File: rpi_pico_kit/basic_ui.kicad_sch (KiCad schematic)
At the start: 48 parts, among them Q3 BSS138, Q4 BSS138, Q5 BSS138, Q6 BSS138, SW2 RotaryEncoder_Switch, SW3 SW_Push, SW4 SW_Push, SW5 SW_Push, SW6 SW_Push, U5 74HC14

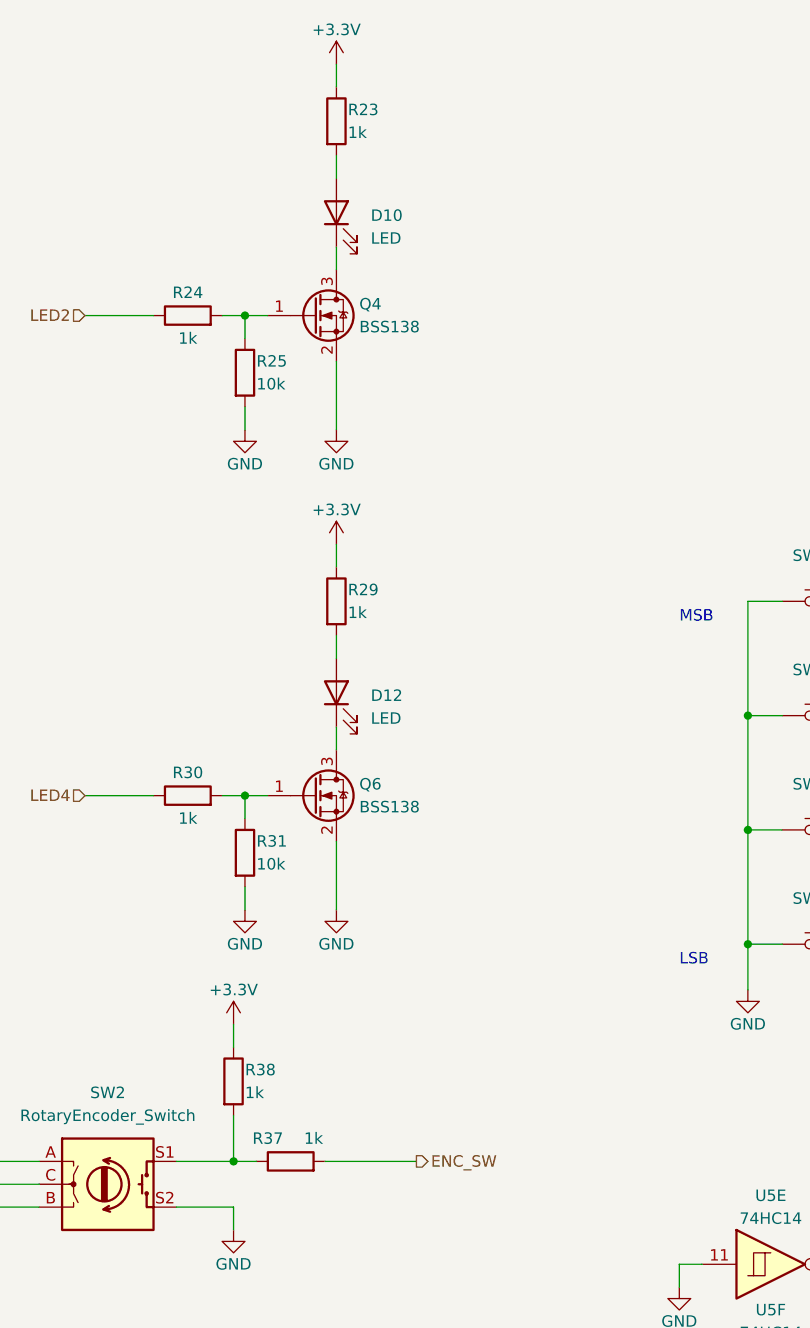
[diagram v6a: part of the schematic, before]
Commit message: changed pinout
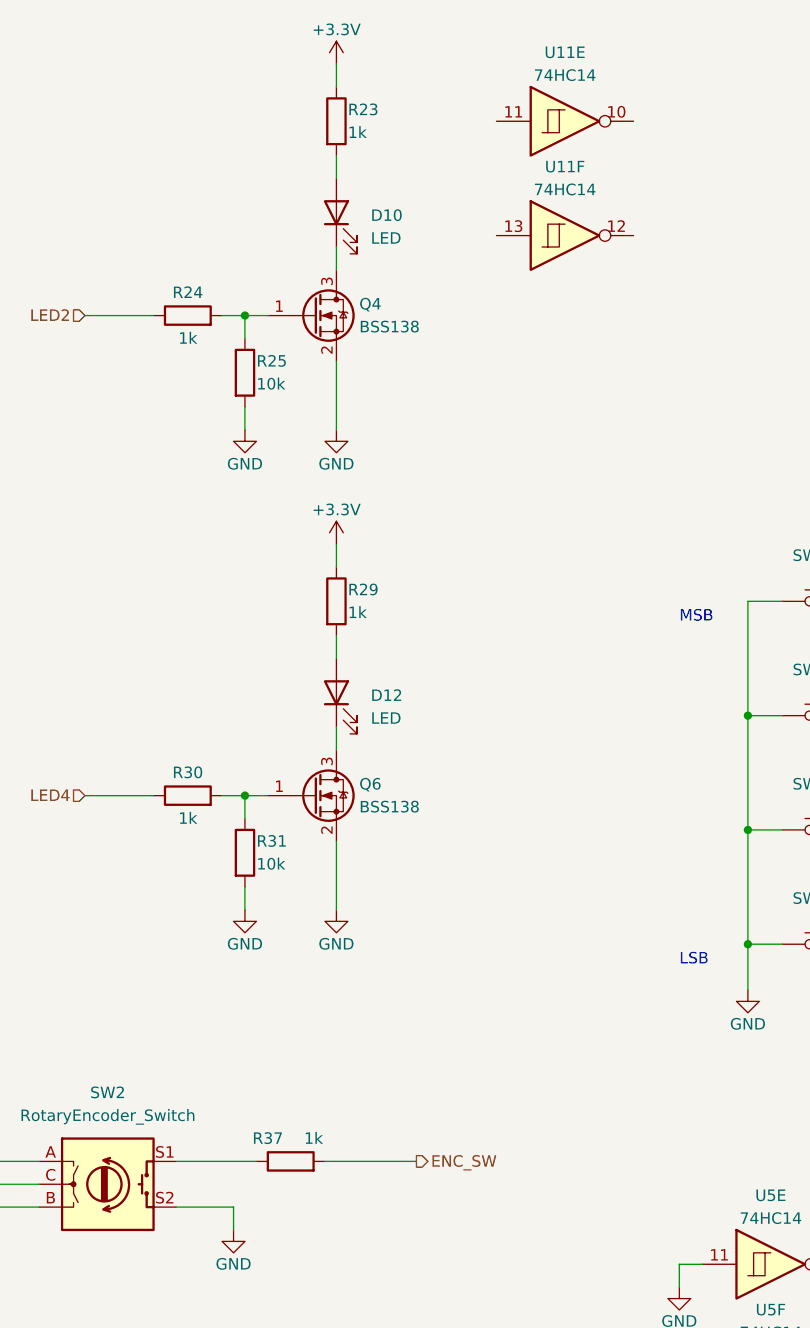
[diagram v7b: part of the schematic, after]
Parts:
- removed R38: 1k, Resistor_SMD:R_0805_2012Metric_Pad1.20x1.40mm_HandSolder, symbol Device:R
- added U11: 74HC14, symbol 74xx:74HC14
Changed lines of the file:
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@@
   (junction (at 185.42 118.11) (diameter 0) (color 0 0 0 0)
-  )
-  (junction (at 91.44 142.24) (diameter 0) (color 0 0 0 0)
   )
   (junction (at 92.71 48.26) (diameter 0) (color 0 0 0 0)
@@
     (stroke (width 0) (type default))
   )
-  (wire (pts (xy 91.44 127) (xy 91.44 129.54))
-    (stroke (width 0) (type default))
-  )
   (wire (pts (xy 102.87 114.3) (xy 102.87 106.68))
     (stroke (width 0) (type default))
@@
     (stroke (width 0) (type default))
   )
-  (wire (pts (xy 91.44 137.16) (xy 91.44 142.24))
-    (stroke (width 0) (type default))
-  )
   (wire (pts (xy 162.56 118.11) (xy 185.42 118.11))
     (stroke (width 0) (type default))
@@
     (stroke (width 0) (type default))
   )
-  (wire (pts (xy 85.09 142.24) (xy 91.44 142.24))
+  (wire (pts (xy 85.09 142.24) (xy 93.98 142.24))
     (stroke (width 0) (type default))
   )
@@
   )
   (wire (pts (xy 172.72 92.71) (xy 193.04 92.71))
-    (stroke (width 0) (type default))
-  )
-  (wire (pts (xy 91.44 142.24) (xy 93.98 142.24))
     (stroke (width 0) (type default))
   )
@@
     (pin "4")
   )
-  (symbol (lib_id "Device:R") (at 91.44 133.35 0) (unit 1)
-    (in_bom yes) (on_board yes)
-    (property "Reference" "R38" (id 0) (at 92.71 132.08 0)
-      (effects (font (size 1.27 1.27)) (justify left))
-    )
-    (property "Value" "1k" (id 1) (at 92.71 134.62 0)
-      (effects (font (size 1.27 1.27)) (justify left))
-    )
-    (property "Footprint" "Resistor_SMD:R_0805_2012Metric_Pad1.20x1.40mm_HandSolder" (id 2) (at 89.662 133.35 90)
-      (effects (font (size 1.27 1.27)) hide)
-    )
-    (property "Datasheet" "~" (id 3) (at 91.44 133.35 0)
-      (effects (font (size 1.27 1.27)) hide)
-    )
-    (pin "1")
-    (pin "2")
-  )
   (symbol (lib_id "Device:R") (at 34.29 101.6 90) (unit 1)
     (in_bom yes) (on_board yes)
@@
     (pin "2")
   )
+  (symbol (lib_id "74xx:74HC14") (at 128.27 26.67 0) (unit 5)
+    (in_bom yes) (on_board yes) (fields_autoplaced)
+    (property "Reference" "U11" (id 0) (at 128.27 19.05 0)
+      (effects (font (size 1.27 1.27)))
+    )
+    (property "Value" "74HC14" (id 1) (at 128.27 21.59 0)
+      (effects (font (size 1.27 1.27)))
+    )
+    (property "Footprint" "" (id 2) (at 128.27 26.67 0)
+      (effects (font (size 1.27 1.27)) hide)
+    )
+    (property "Datasheet" "http://www.ti.com/lit/gpn/sn74HC14" (id 3) (at 128.27 26.67 0)
+      (effects (font (size 1.27 1.27)) hide)
+    )
+    (pin "10")
+    (pin "11")
+  )
   (symbol (lib_id "power:GND") (at 267.97 95.25 0) (unit 1)
     (in_bom yes) (on_board yes)
@@
     (pin "1")
   )
-  (symbol (lib_id "power:+3.3V") (at 91.44 127 0) (unit 1)
-    (in_bom yes) (on_board yes)
-    (property "Reference" "#PWR055" (id 0) (at 91.44 130.81 0)
-      (effects (font (size 1.27 1.27)) hide)
-    )
-    (property "Value" "+3.3V" (id 1) (at 91.44 123.19 0)
-      (effects (font (size 1.27 1.27)))
-    )
-    (property "Footprint" "" (id 2) (at 91.44 127 0)
-      (effects (font (size 1.27 1.27)) hide)
-    )
-    (property "Datasheet" "" (id 3) (at 91.44 127 0)
-      (effects (font (size 1.27 1.27)) hide)
-    )
-    (pin "1")
-  )
   (symbol (lib_id "74xx:74HC14") (at 200.66 118.11 0) (unit 4)
     (in_bom yes) (on_board yes) (fields_autoplaced)
@@
     (pin "1")
   )
+  (symbol (lib_id "74xx:74HC14") (at 128.27 39.37 0) (unit 6)
+    (in_bom yes) (on_board yes) (fields_autoplaced)
+    (property "Reference" "U11" (id 0) (at 128.27 31.75 0)
+      (effects (font (size 1.27 1.27)))
+    )
+    (property "Value" "74HC14" (id 1) (at 128.27 34.29 0)
+      (effects (font (size 1.27 1.27)))
+    )
+    (property "Footprint" "" (id 2) (at 128.27 39.37 0)
+      (effects (font (size 1.27 1.27)) hide)
+    )
+    (property "Datasheet" "http://www.ti.com/lit/gpn/sn74HC14" (id 3) (at 128.27 39.37 0)
+      (effects (font (size 1.27 1.27)) hide)
+    )
+    (pin "12")
+    (pin "13")
+  )
   (symbol (lib_id "74xx:74HC14") (at 200.66 105.41 0) (unit 3)

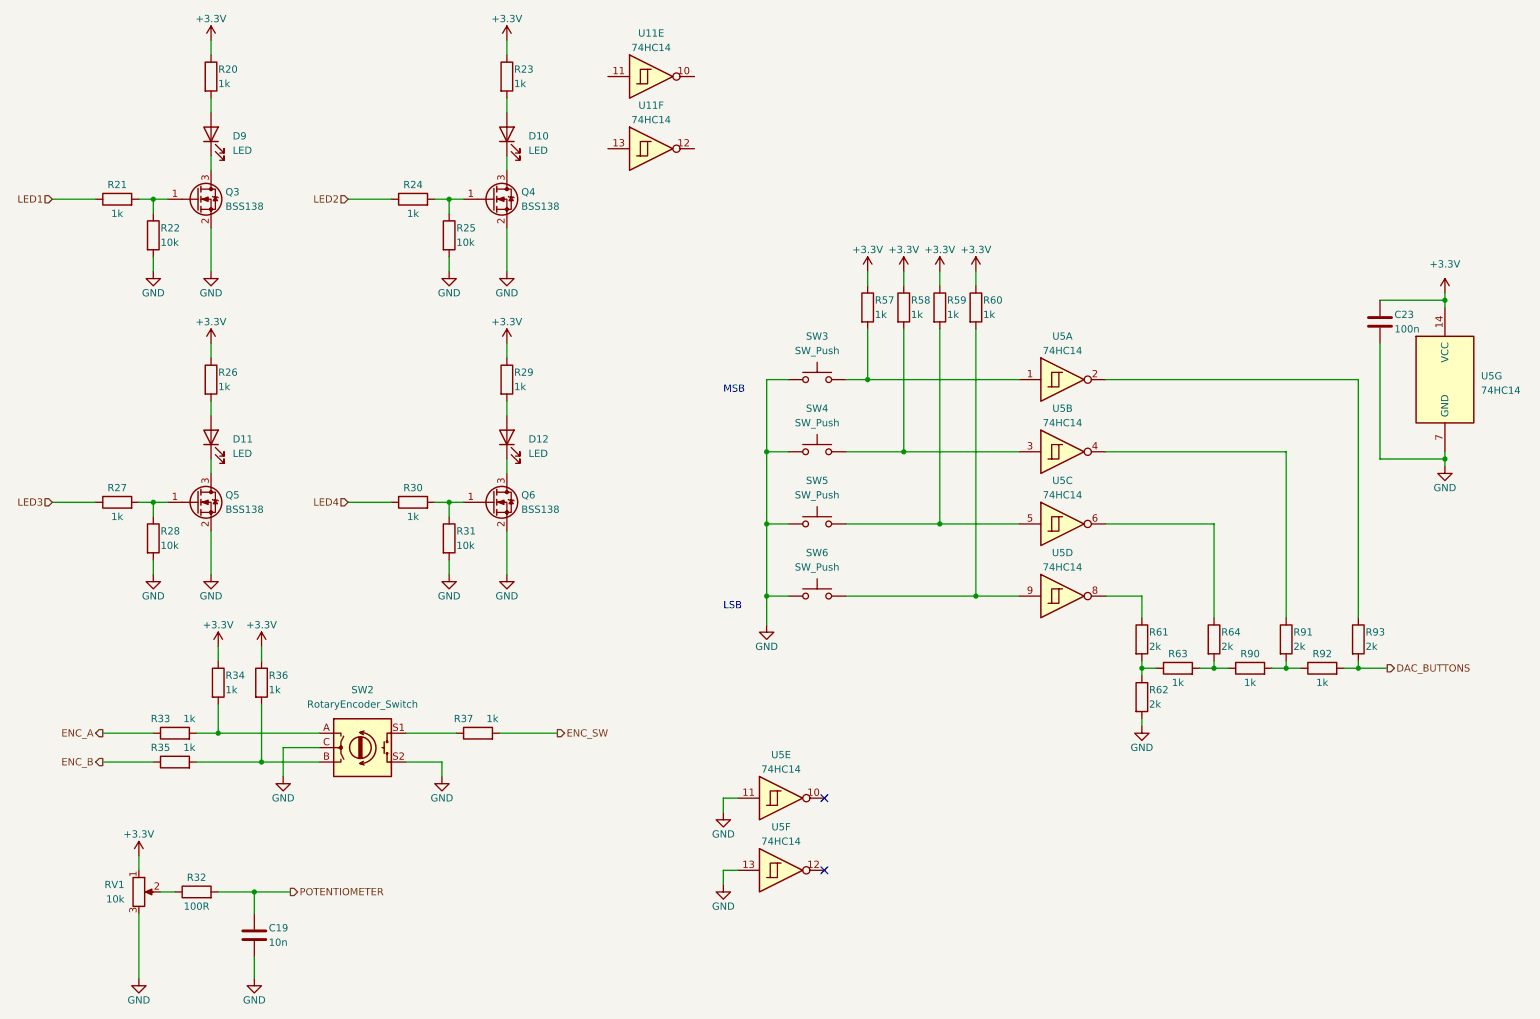
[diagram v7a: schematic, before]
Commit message: changed transistors to unused gates of 7414
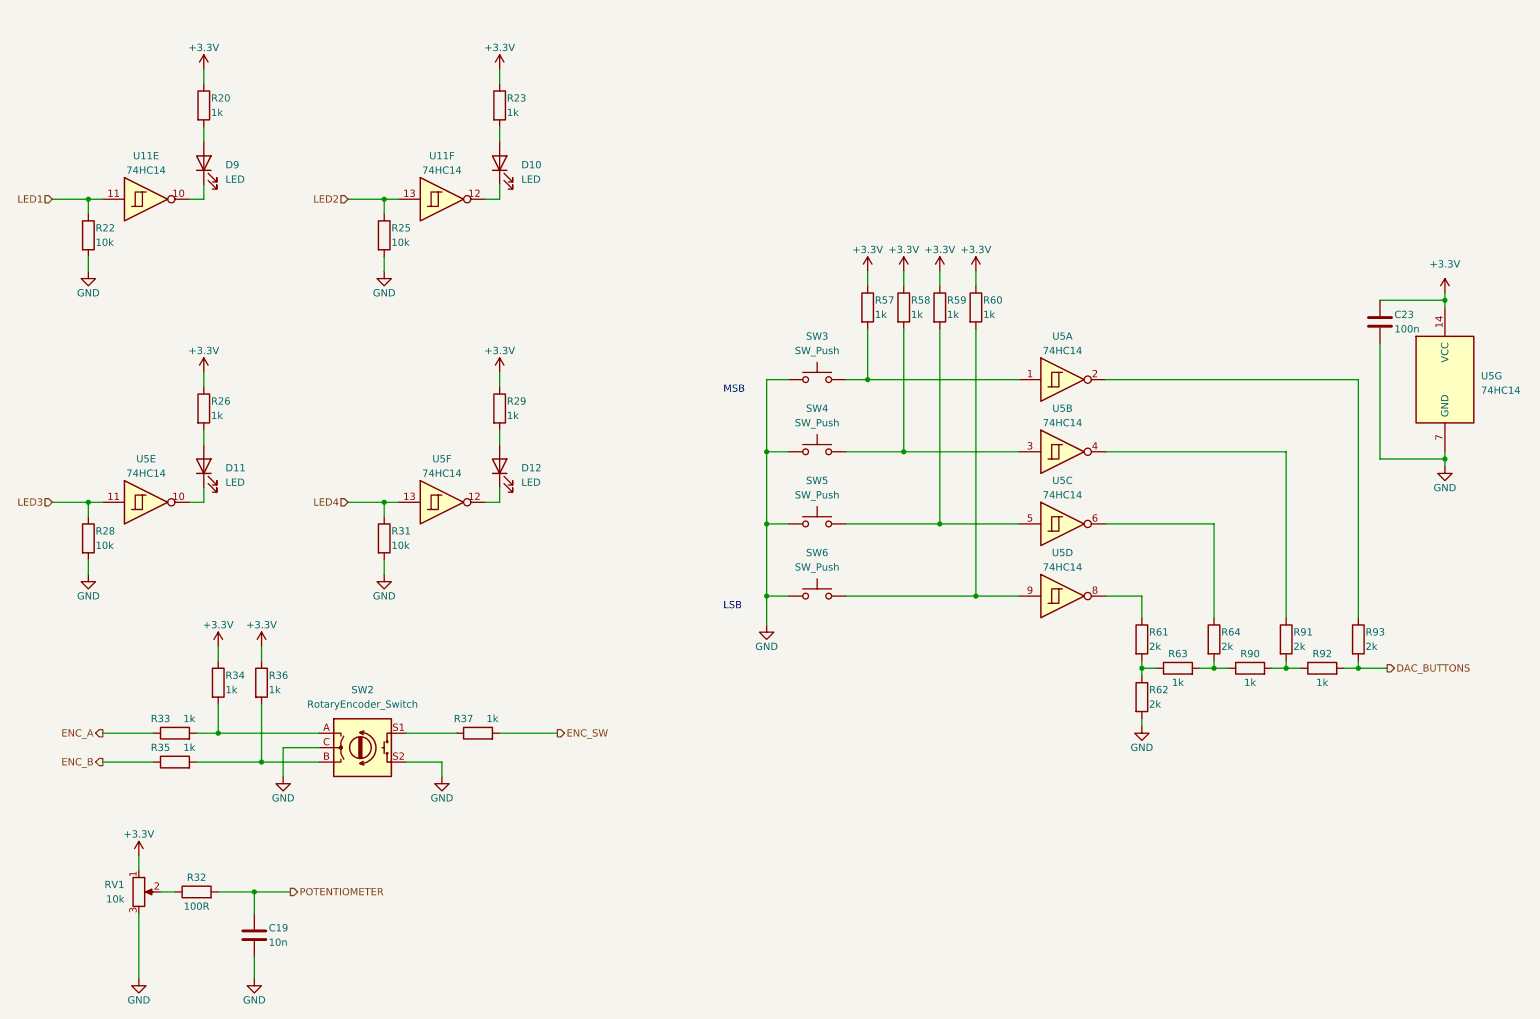
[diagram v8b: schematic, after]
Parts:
- removed Q3, Q4, Q5, Q6: BSS138, Package_TO_SOT_SMD:SOT-23, symbol Transistor_FET:BSS138
- removed R21, R24, R27, R30: 1k, Resistor_SMD:R_0805_2012Metric_Pad1.20x1.40mm_HandSolder, symbol Device:R
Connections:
- net GND: no longer U5.11, U5.13
- net LED1: now also R22.1, U11.11
- net LED2: now also R25.1, U11.13
- net LED3: now also R28.1, U5.11
- net LED4: now also R31.1, U5.13
- net at D9.1 (K): now also U11.10
- net at D10.1 (K): now also U11.12
- net at D11.1 (K): now also U5.10
- net at D12.1 (K): now also U5.12
- no-connect marks 2 -> 0
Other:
- moved on the sheet: D10, D11, D12, D9, R20, R22, R23, R25, R26, R28, R29, R31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
